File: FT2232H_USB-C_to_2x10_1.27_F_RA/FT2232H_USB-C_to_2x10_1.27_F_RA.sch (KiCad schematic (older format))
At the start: 33 parts

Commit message: Initial placement for FT2232H_USB-C
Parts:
- removed C?: 4u7, symbol Device:C
- removed C?: 100n, symbol Device:C
- removed J?: USB_B_Micro, symbol ng_conn:USB_B_Micro
- removed L? (x2): 600R, symbol Device:L
- removed R?: 1M, symbol Device:R
- added C20, C5: 4u7, Capacitor_SMD:C_0603_1608Metric, symbol Device:C
- added C21, C3, C4: 100n, Capacitor_SMD:C_0603_1608Metric, symbol Device:C
- added C6: 10n, Capacitor_SMD:C_0603_1608Metric, symbol Device:C
- added FB1: 33R, 3A, Inductor_SMD:L_0603_1608Metric, symbol Device:Ferrite_Bead
- added FB2, FB3: 600R, Inductor_SMD:L_0603_1608Metric, symbol Device:Ferrite_Bead
- added J1: USB_B_Micro, Connector_USB:USB_Micro-B_Molex_47346-0001, symbol ng_conn:USB_B_Micro
- added J2, J3: Conn_02x10_Odd_Even, Connector_PinSocket_2.54mm:PinSocket_2x10_P2.54mm_Horizontal, symbol Connector_Generic:Conn_02x10_Odd_Even
- added R1: 100k, Resistor_SMD:R_0603_1608Metric, symbol Device:R
- added unit 4 of R4
- added U3: USBLC6-2SC6, Package_TO_SOT_SMD:SOT-23-6, symbol Power_Protection:USBLC6-2SC6
- C1, C10, C11, C12, C13, C14, C15, C16, C17, C18, C19, C2, C7, C8, C9: renamed from C?; footprint (none) -> Capacitor_SMD:C_0603_1608Metric
- D1: renamed from D?; footprint (none) -> LED_SMD:LED_0603_1608Metric; MPN HSMG-C190 -> (none)
- R2, R5, R6: renamed from R?; footprint (none) -> Resistor_SMD:R_0603_1608Metric
- R3: renamed from R?; value 12k 1% -> 12k, 1%; footprint (none) -> Resistor_SMD:R_0603_1608Metric
- R4: renamed from R?; footprint (none) -> Resistor_SMD:R_Array_Convex_4x0603; MPN (none) -> YC164-JR-0710KL
- R4: renamed from R?; footprint (none) -> Resistor_SMD:R_Array_Convex_4x0603
- U1: renamed from U?; value FT2232H -> FT2232HL; footprint (none) -> Package_QFP:LQFP-64_10x10mm_P0.5mm
- X1: renamed from X?; footprint (none) -> ng_time:Oscillator_2.5x2.0
- gave numbers to parts that had none: 2
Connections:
- net labels added: P1V8, P3V3, USB_5V, USB_EECLK, USB_EECS, USB_EEDATA, USB_EEDO, USB_OSC, USB_SHD, USB_VBUS, xUSB_D+, xUSB_D-
- net labels removed: +1V8, +3V3, +5V
- wire segments 195 -> 260
- no-connect marks 4 -> 6
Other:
- note added: "USBLC6 requires 100n (C18) on VBUS,\nnot 10n as would be expected"
- note removed: "Adapter Headers"
- note removed: "FTDI Programmer / UART"
- note removed: "Power"
- note removed: "Status LEDs"
- moved on the sheet: C1, C10, C11, C12, C13, C14, C15, C16, C17, C18, C19, C2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

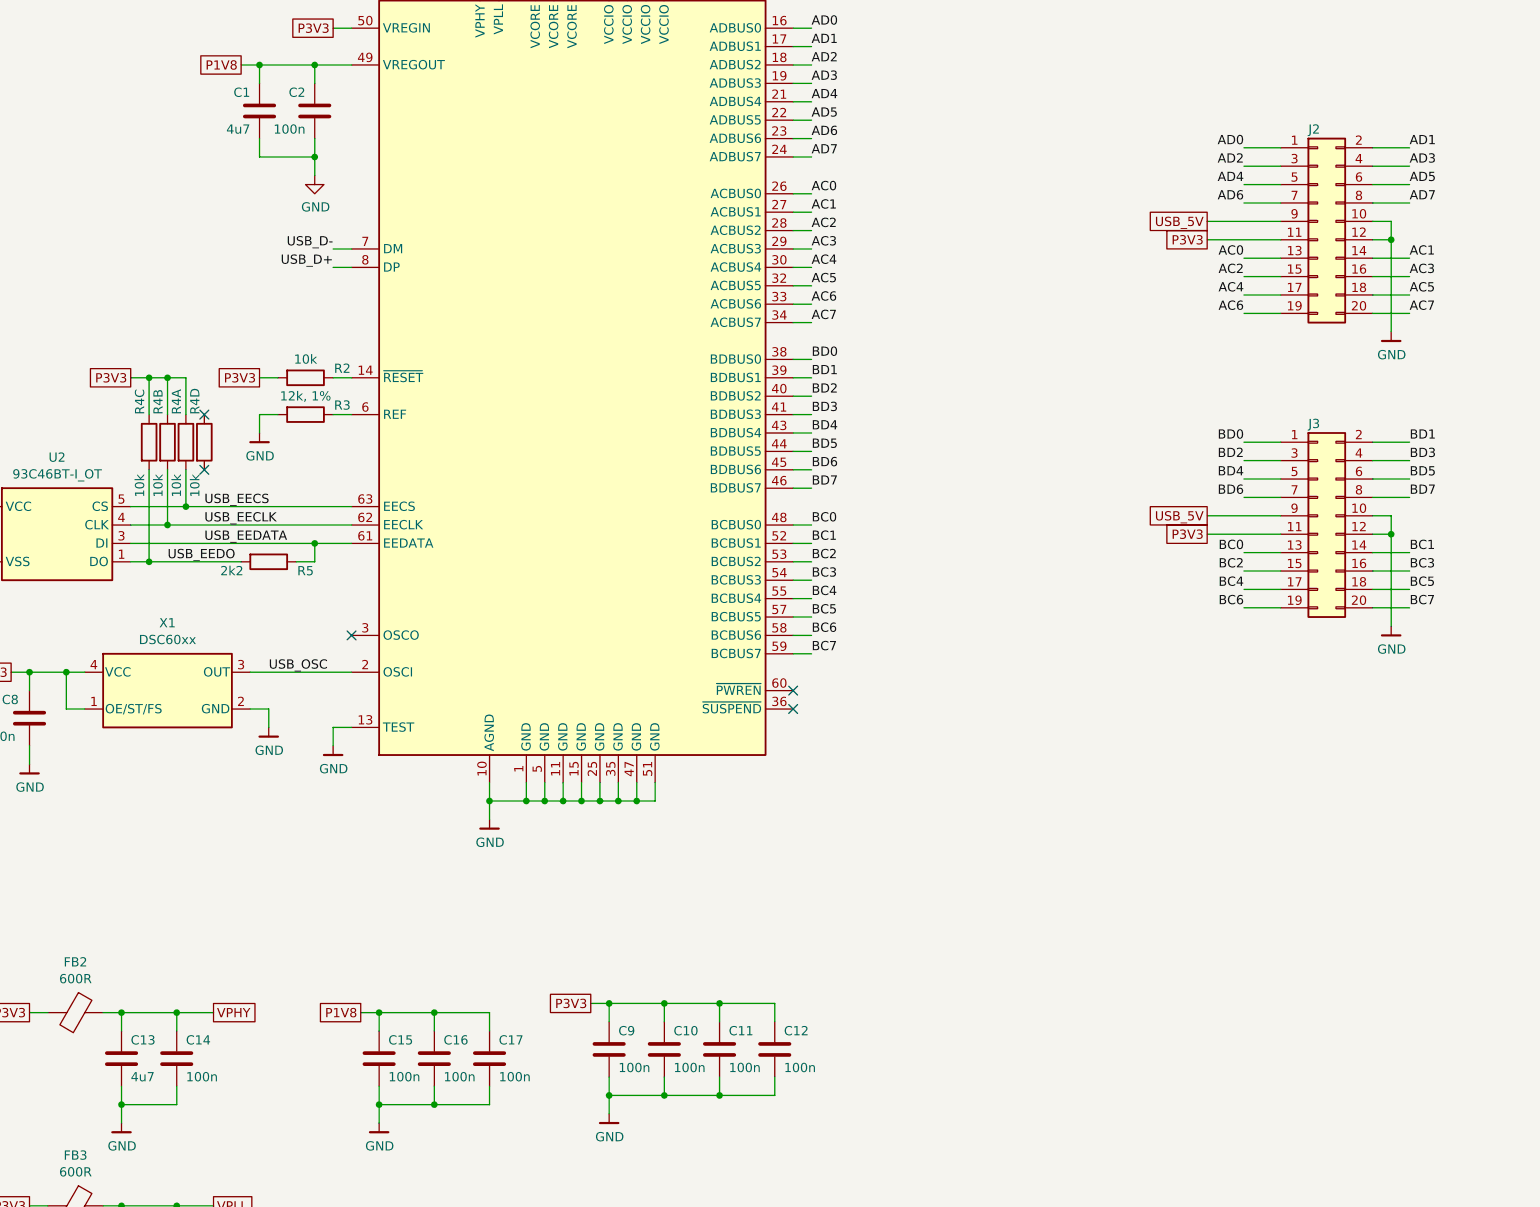
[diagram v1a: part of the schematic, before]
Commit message: Adjusting placement for FT2232_USB-C
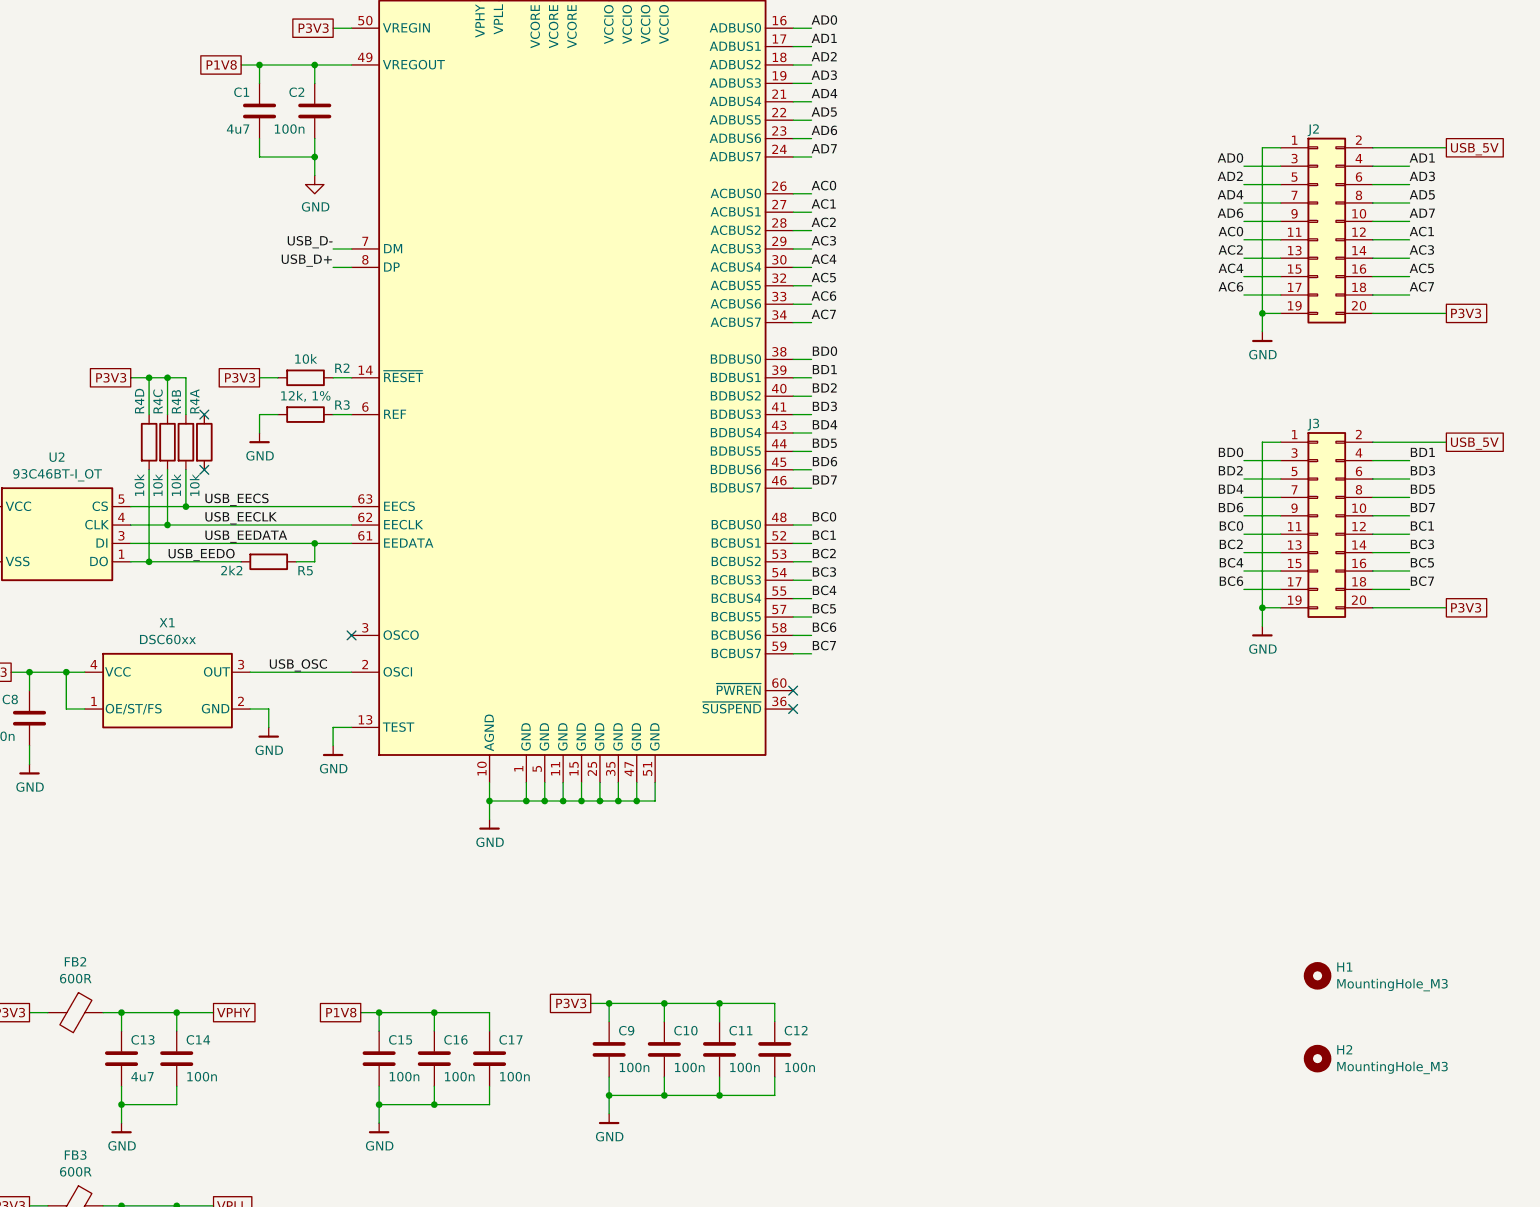
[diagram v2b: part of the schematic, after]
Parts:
- added H1, H2: MountingHole_M3, MountingHole:MountingHole_3.2mm_M3, symbol Mechanical:MountingHole
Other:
- moved on the sheet: R4A, R4B, R4C, R4D
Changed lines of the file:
@@
 L Device:R_Pack04_Split R4
 U 1 1 5F1F46F9
+P 7600 4900
+F 0 "R4" V 7550 5050 50  0000 L CNN
+F 1 "10k" V 7550 4600 50  0000 L CNN
+F 2 "Resistor_SMD:R_Array_Convex_4x0603" V 7530 4900 50  0001 C CNN
+F 3 "~" H 7600 4900 50  0001 C CNN
+F 4 "YC164-JR-0710KL" V 7600 4900 50  0001 C CNN "MPN"
+	1    7600 4900
+	1    0    0    -1
+$EndComp
+$Comp
+L Device:R_Pack04_Split R4
+U 3 1 5F1F46FF
+P 7400 4900
+F 0 "R4" V 7350 5050 50  0000 L CNN
+F 1 "10k" V 7350 4600 50  0000 L CNN
+F 2 "Resistor_SMD:R_Array_Convex_4x0603" V 7330 4900 50  0001 C CNN
+F 3 "~" H 7400 4900 50  0001 C CNN
+	3    7400 4900
+	1    0    0    -1
+$EndComp
+$Comp
+L Device:R_Pack04_Split R4
+U 2 1 5F1F4705
 P 7500 4900
 F 0 "R4" V 7450 5050 50  0000 L CNN
@@
 F 2 "Resistor_SMD:R_Array_Convex_4x0603" V 7430 4900 50  0001 C CNN
 F 3 "~" H 7500 4900 50  0001 C CNN
-F 4 "YC164-JR-0710KL" V 7500 4900 50  0001 C CNN "MPN"
-	1    7500 4900
-	1    0    0    -1
-$EndComp
-$Comp
-L Device:R_Pack04_Split R4
-U 3 1 5F1F46FF
-P 7300 4900
-F 0 "R4" V 7250 5050 50  0000 L CNN
-F 1 "10k" V 7250 4600 50  0000 L CNN
-F 2 "Resistor_SMD:R_Array_Convex_4x0603" V 7230 4900 50  0001 C CNN
-F 3 "~" H 7300 4900 50  0001 C CNN
-	3    7300 4900
-	1    0    0    -1
-$EndComp
-$Comp
-L Device:R_Pack04_Split R4
-U 2 1 5F1F4705
-P 7400 4900
-F 0 "R4" V 7350 5050 50  0000 L CNN
-F 1 "10k" V 7350 4600 50  0000 L CNN
-F 2 "Resistor_SMD:R_Array_Convex_4x0603" V 7330 4900 50  0001 C CNN
-F 3 "~" H 7400 4900 50  0001 C CNN
-	2    7400 4900
+	2    7500 4900
 	1    0    0    -1
 $EndComp
@@
 $EndComp
 Wire Wire Line
-	13450 3300 13250 3300
-Wire Wire Line
-	14150 3300 13950 3300
+	13450 3400 13250 3400
 Wire Wire Line
 	14150 3400 13950 3400
@@
 	14150 3600 13950 3600
 Wire Wire Line
-	14050 3700 13950 3700
-Wire Wire Line
-	14050 3800 13950 3800
+	14150 3700 13950 3700
+Wire Wire Line
+	14150 3800 13950 3800
 Wire Wire Line
 	14150 3900 13950 3900
@@
 Wire Wire Line
 	14150 4100 13950 4100
-Wire Wire Line
-	14150 4200 13950 4200
-Text Label 13250 3300 2    50   ~ 0
+Text Label 13250 3400 2    50   ~ 0
 AD0
-Text Label 14150 3300 0    50   ~ 0
+Text Label 14150 3400 0    50   ~ 0
 AD1
-Text Label 13250 3400 2    50   ~ 0
+Text Label 13250 3500 2    50   ~ 0
 AD2
-Text Label 14150 3400 0    50   ~ 0
+Text Label 14150 3500 0    50   ~ 0
 AD3
-Text Label 13250 3500 2    50   ~ 0
+Text Label 13250 3600 2    50   ~ 0
 AD4
-Text Label 14150 3500 0    50   ~ 0
+Text Label 14150 3600 0    50   ~ 0
 AD5
-Text Label 13250 3600 2    50   ~ 0
+Text Label 13250 3700 2    50   ~ 0
 AD6
-Text Label 14150 3600 0    50   ~ 0
+Text Label 14150 3700 0    50   ~ 0
 AD7
+Text Label 13250 3800 2    50   ~ 0
+AC0
+Text Label 14150 3800 0    50   ~ 0
+AC1
 Text Label 13250 3900 2    50   ~ 0
-AC0
+AC2
 Text Label 14150 3900 0    50   ~ 0
-AC1
+AC3
 Text Label 13250 4000 2    50   ~ 0
-AC2
+AC4
 Text Label 14150 4000 0    50   ~ 0
-AC3
+AC5
 Text Label 13250 4100 2    50   ~ 0
-AC4
+AC6
 Text Label 14150 4100 0    50   ~ 0
-AC5
-Text Label 13250 4200 2    50   ~ 0
-AC6
-Text Label 14150 4200 0    50   ~ 0
 AC7
-Wire Wire Line
-	14050 3700 14050 3800
-Connection ~ 14050 3800
-Wire Wire Line
-	14050 3800 14050 4300
 $Comp
 L ng_power:GND #PWR0120
 U 1 1 5F84B027
-P 14050 4300
-F 0 "#PWR0120" H 14050 4050 50  0001 C CNN
-F 1 "GND" H 14053 4174 50  0000 C CNN
-F 2 "" H 13950 3950 50  0001 C CNN
-F 3 "" H 14050 4300 50  0001 C CNN
-	1    14050 4300
-	1    0    0    -1
-$EndComp
-Text GLabel 13050 3700 0    50   UnSpc ~ 0
+P 13350 4300
+F 0 "#PWR0120" H 13350 4050 50  0001 C CNN
+F 1 "GND" H 13353 4174 50  0000 C CNN
+F 2 "" H 13250 3950 50  0001 C CNN
+F 3 "" H 13350 4300 50  0001 C CNN
+	1    13350 4300
+	1    0    0    -1
+$EndComp
+Text GLabel 14350 3300 2    50   UnSpc ~ 0
 USB_5V
-Text GLabel 13050 3800 0    50   UnSpc ~ 0
+Text GLabel 14350 4200 2    50   UnSpc ~ 0
 P3V3
 Wire Wire Line
-	13250 3400 13450 3400
-Wire Wire Line
 	13250 3500 13450 3500
 Wire Wire Line
 	13250 3600 13450 3600
 Wire Wire Line
-	13050 3700 13450 3700
-Wire Wire Line
-	13050 3800 13450 3800
+	13250 3700 13450 3700
+Wire Wire Line
+	14350 3300 13950 3300
+Wire Wire Line
+	14350 4200 13950 4200
+Wire Wire Line
+	13250 3800 13450 3800
 Wire Wire Line
 	13250 3900 13450 3900
@@
 Wire Wire Line
 	13250 4100 13450 4100
-Wire Wire Line
-	13250 4200 13450 4200
 $Comp
 L Connector_Generic:Conn_02x10_Odd_Even J3
@@
 $EndComp
 Wire Wire Line
-	13450 4900 13250 4900
-Wire Wire Line
-	14150 4900 13950 4900
+	13450 5000 13250 5000
 Wire Wire Line
 	14150 5000 13950 5000
@@
 	14150 5200 13950 5200
 Wire Wire Line
-	14050 5300 13950 5300
-Wire Wire Line
-	14050 5400 13950 5400
+	14150 5300 13950 5300
+Wire Wire Line
+	14150 5400 13950 5400
 Wire Wire Line
 	14150 5500 13950 5500
@@
 Wire Wire Line
 	14150 5700 13950 5700
-Wire Wire Line
-	14150 5800 13950 5800
-Text Label 13250 4900 2    50   ~ 0
+Text Label 13250 5000 2    50   ~ 0
 BD0
-Text Label 14150 4900 0    50   ~ 0
+Text Label 14150 5000 0    50   ~ 0
 BD1
-Text Label 13250 5000 2    50   ~ 0
+Text Label 13250 5100 2    50   ~ 0
 BD2
-Text Label 14150 5000 0    50   ~ 0
+Text Label 14150 5100 0    50   ~ 0
 BD3
-Text Label 13250 5100 2    50   ~ 0
+Text Label 13250 5200 2    50   ~ 0
 BD4
-Text Label 14150 5100 0    50   ~ 0
+Text Label 14150 5200 0    50   ~ 0
 BD5
-Text Label 13250 5200 2    50   ~ 0
+Text Label 13250 5300 2    50   ~ 0
 BD6
-Text Label 14150 5200 0    50   ~ 0
+Text Label 14150 5300 0    50   ~ 0
 BD7
+Text Label 13250 5400 2    50   ~ 0
+BC0
+Text Label 14150 5400 0    50   ~ 0
+BC1
 Text Label 13250 5500 2    50   ~ 0
-BC0
+BC2
 Text Label 14150 5500 0    50   ~ 0
-BC1
+BC3
 Text Label 13250 5600 2    50   ~ 0
-BC2
+BC4
 Text Label 14150 5600 0    50   ~ 0
-BC3
+BC5
 Text Label 13250 5700 2    50   ~ 0
-BC4
+BC6
 Text Label 14150 5700 0    50   ~ 0
-BC5
-Text Label 13250 5800 2    50   ~ 0
-BC6
-Text Label 14150 5800 0    50   ~ 0
 BC7
-Wire Wire Line
-	14050 5300 14050 5400
-Connection ~ 14050 5400
-Wire Wire Line
-	14050 5400 14050 5900
 $Comp
 L ng_power:GND #PWR0121
 U 1 1 5F936E43
-P 14050 5900
-F 0 "#PWR0121" H 14050 5650 50  0001 C CNN
-F 1 "GND" H 14053 5774 50  0000 C CNN
-F 2 "" H 13950 5550 50  0001 C CNN
-F 3 "" H 14050 5900 50  0001 C CNN
-	1    14050 5900
-	1    0    0    -1
-$EndComp
-Text GLabel 13050 5300 0    50   UnSpc ~ 0
+P 13350 5900
+F 0 "#PWR0121" H 13350 5650 50  0001 C CNN
+F 1 "GND" H 13353 5774 50  0000 C CNN
+F 2 "" H 13250 5550 50  0001 C CNN
+F 3 "" H 13350 5900 50  0001 C CNN
+	1    13350 5900
+	1    0    0    -1
+$EndComp
+Text GLabel 14350 4900 2    50   UnSpc ~ 0
 USB_5V
-Text GLabel 13050 5400 0    50   UnSpc ~ 0
+Text GLabel 14350 5800 2    50   UnSpc ~ 0
 P3V3
 Wire Wire Line
-	13250 5000 13450 5000
-Wire Wire Line
 	13250 5100 13450 5100
 Wire Wire Line
 	13250 5200 13450 5200
 Wire Wire Line
-	13050 5300 13450 5300
-Wire Wire Line
-	13050 5400 13450 5400
+	13250 5300 13450 5300
+Wire Wire Line
+	14350 4900 13950 4900
+Wire Wire Line
+	14350 5800 13950 5800
+Wire Wire Line
+	13250 5400 13450 5400
 Wire Wire Line
 	13250 5500 13450 5500
@@
 Wire Wire Line
 	13250 5700 13450 5700
-Wire Wire Line
-	13250 5800 13450 5800
 Wire Wire Line
 	3250 3650 3750 3650
@@
 L Device:R_Pack04_Split R4
 U 4 1 5FBDF481
-P 7600 4900
-F 0 "R4" V 7550 5050 50  0000 L CNN
-F 1 "10k" V 7550 4600 50  0000 L CNN
-F 2 "Resistor_SMD:R_Array_Convex_4x0603" V 7530 4900 50  0001 C CNN
-F 3 "~" H 7600 4900 50  0001 C CNN
-F 4 "YC164-JR-0710KL" V 7600 4900 50  0001 C CNN "MPN"
-	4    7600 4900
-	1    0    0    -1
-$EndComp
+P 7300 4900
+F 0 "R4" V 7250 5050 50  0000 L CNN
+F 1 "10k" V 7250 4600 50  0000 L CNN
+F 2 "Resistor_SMD:R_Array_Convex_4x0603" V 7230 4900 50  0001 C CNN
+F 3 "~" H 7300 4900 50  0001 C CNN
+F 4 "YC164-JR-0710KL" V 7300 4900 50  0001 C CNN "MPN"
+	4    7300 4900
+	1    0    0    -1
+$EndComp
+$Comp
+L Mechanical:MountingHole H1
+U 1 1 5FCF15CE
+P 13650 7800
+F 0 "H1" H 13750 7846 50  0000 L CNN
+F 1 "MountingHole_M3" H 13750 7755 50  0000 L CNN
+F 2 "MountingHole:MountingHole_3.2mm_M3" H 13650 7800 50  0001 C CNN
+F 3 "~" H 13650 7800 50  0001 C CNN
+	1    13650 7800
+	1    0    0    -1
+$EndComp
+$Comp
+L Mechanical:MountingHole H2
+U 1 1 5FCF2040
+P 13650 8250
+F 0 "H2" H 13750 8296 50  0000 L CNN
+F 1 "MountingHole_M3" H 13750 8205 50  0000 L CNN
+F 2 "MountingHole:MountingHole_3.2mm_M3" H 13650 8250 50  0001 C CNN
+F 3 "~" H 13650 8250 50  0001 C CNN
+	1    13650 8250
+	1    0    0    -1
+$EndComp
+Wire Wire Line
+	13350 4300 13350 4200
+Wire Wire Line
+	13350 3300 13450 3300
+Wire Wire Line
+	13450 4200 13350 4200
+Connection ~ 13350 4200
+Wire Wire Line
+	13350 4200 13350 3300
+Wire Wire Line
+	13350 5900 13350 5800
+Wire Wire Line
+	13350 4900 13450 4900
+Wire Wire Line
+	13450 5800 13350 5800
+Connection ~ 13350 5800
+Wire Wire Line
+	13350 5800 13350 4900
 $EndSCHEMATC

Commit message: Add Nelgau-Logo to FT2232H_USB-C
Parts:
- added SYM1: Nelgau-Logo, ng_symbol:Nelgau-Logo_5.2x1.7mm_SilkScreen, symbol ng_symbol:Symbol
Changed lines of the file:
@@
 Wire Wire Line
 	13350 5800 13350 4900
+$Comp
+L ng_symbol:Symbol SYM1
+U 1 1 5FF0B0EB
+P 13650 8650
+F 0 "SYM1" H 13735 8696 50  0000 L CNN
+F 1 "Nelgau-Logo" H 13735 8605 50  0000 L CNN
+F 2 "ng_symbol:Nelgau-Logo_5.2x1.7mm_SilkScreen" H 13650 8650 50  0001 C CNN
+F 3 "" H 13650 8650 50  0001 C CNN
+	1    13650 8650
+	1    0    0    -1
+$EndComp
 $EndSCHEMATC

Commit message: Add tentative board edge and trim pin socket footprints
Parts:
- J2, J3: footprint Connector_PinSocket_2.54mm:PinSocket_2x10_P2.54mm_Horizontal -> local_conn:PinSocket_2x10_P2.54mm_Horizontal
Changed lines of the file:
@@
 F 0 "J2" H 13600 4200 50  0000 L CNN
 F 1 "Conn_02x10_Odd_Even" H 13700 4226 50  0001 C CNN
-F 2 "Connector_PinSocket_2.54mm:PinSocket_2x10_P2.54mm_Horizontal" H 13650 3700 50  0001 C CNN
+F 2 "local_conn:PinSocket_2x10_P2.54mm_Horizontal" H 13650 3700 50  0001 C CNN
 F 3 "~" H 13650 3700 50  0001 C CNN
 	1    13650 3700
@@
 F 0 "J3" H 13600 5800 50  0000 L CNN
 F 1 "Conn_02x10_Odd_Even" H 13700 5826 50  0001 C CNN
-F 2 "Connector_PinSocket_2.54mm:PinSocket_2x10_P2.54mm_Horizontal" H 13650 5300 50  0001 C CNN
+F 2 "local_conn:PinSocket_2x10_P2.54mm_Horizontal" H 13650 5300 50  0001 C CNN
 F 3 "~" H 13650 5300 50  0001 C CNN
 	1    13650 5300

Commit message: Use USB-C connector instead of micro-USB
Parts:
- removed J1: USB_B_Micro, Connector_USB:USB_Micro-B_Molex_47346-0001, symbol ng_conn:USB_B_Micro
- added J1: USB_C_USB2.0, ng_conn:USB_C_Receptacle_HRO_TYPE-C-31-M-12, symbol Connector:USB_C_Receptacle_USB2.0
- added R7, R8: 5k1, Resistor_SMD:R_0603_1608Metric, symbol Device:R
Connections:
- net labels added: USB_CC1, USB_CC2
- wire segments 260 -> 273
- no-connect marks 6 -> 7
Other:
- moved on the sheet: C3, C4, C5, C6, FB1, R1, U3

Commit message: Implement option to use LDO with bypass capacitor
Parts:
- removed U4: MIC5504-3.3YM5, Package_TO_SOT_SMD:SOT-23-5, symbol ng_regulator:MIC5504-3.3YM5
- added C22: 10n, Capacitor_SMD:C_0603_1608Metric, symbol Device:C
- added U4: LDO_SOT-23-5, Package_TO_SOT_SMD:SOT-23-5, symbol ng_regulator:LDO_SOT-23-5
- C19: value 100n -> 4u7
- H1, H2: footprint MountingHole:MountingHole_3.2mm_M3 -> MountingHole:MountingHole_3.2mm_M3_Pad_Via; symbol Mechanical:MountingHole -> Mechanical:MountingHole_Pad
- R2: value 10k -> 1k
- R6: value 249R -> 1k
- X1: Freq (none) -> 12 MHz
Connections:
- net GND: now also H1.1, H2.1, C22.2, U4.2 (GND)
- net P3V3: now also U4.5 (OUT)
- net USB_5V: now also U4.1 (IN), U4.3 (EN)
- net USB_OSC renamed USB_CLK
- new net: C22.1, U4.4 (BP)
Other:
- note added: "+/-30ppm, <150pS"
- moved on the sheet: C18, C19, D1, R6, SYM1

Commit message: Poor copper zones and run final DRC checks
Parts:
- R4: symbol Device:R_Pack04_Split -> FT2232H_USB-C_to_2x10_1.27_F_RA-rescue:R_Pack04_Split-Device
- U3: symbol Power_Protection:USBLC6-2SC6 -> FT2232H_USB-C_to_2x10_1.27_F_RA-rescue:USBLC6-2SC6-Power_Protection
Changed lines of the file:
@@
 	7500 5250 7500 5050
 $Comp
-L Device:R_Pack04_Split R4
+L FT2232H_USB-C_to_2x10_1.27_F_RA-rescue:R_Pack04_Split-Device R4
 U 1 1 5F1F46F9
 P 7600 4900
@@
 $EndComp
 $Comp
-L Device:R_Pack04_Split R4
+L FT2232H_USB-C_to_2x10_1.27_F_RA-rescue:R_Pack04_Split-Device R4
 U 3 1 5F1F46FF
 P 7400 4900
@@
 $EndComp
 $Comp
-L Device:R_Pack04_Split R4
+L FT2232H_USB-C_to_2x10_1.27_F_RA-rescue:R_Pack04_Split-Device R4
 U 2 1 5F1F4705
 P 7500 4900
@@
 	3350 4800 3800 4800
 $Comp
-L Power_Protection:USBLC6-2SC6 U?
+L FT2232H_USB-C_to_2x10_1.27_F_RA-rescue:USBLC6-2SC6-Power_Protection U?
 U 1 1 5F184C87
 P 3800 5400
@@
 NoConn ~ 7600 4750
 $Comp
-L Device:R_Pack04_Split R4
+L FT2232H_USB-C_to_2x10_1.27_F_RA-rescue:R_Pack04_Split-Device R4
 U 4 1 5FBDF481
 P 7300 4900
